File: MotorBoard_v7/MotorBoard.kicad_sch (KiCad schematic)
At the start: 4 parts

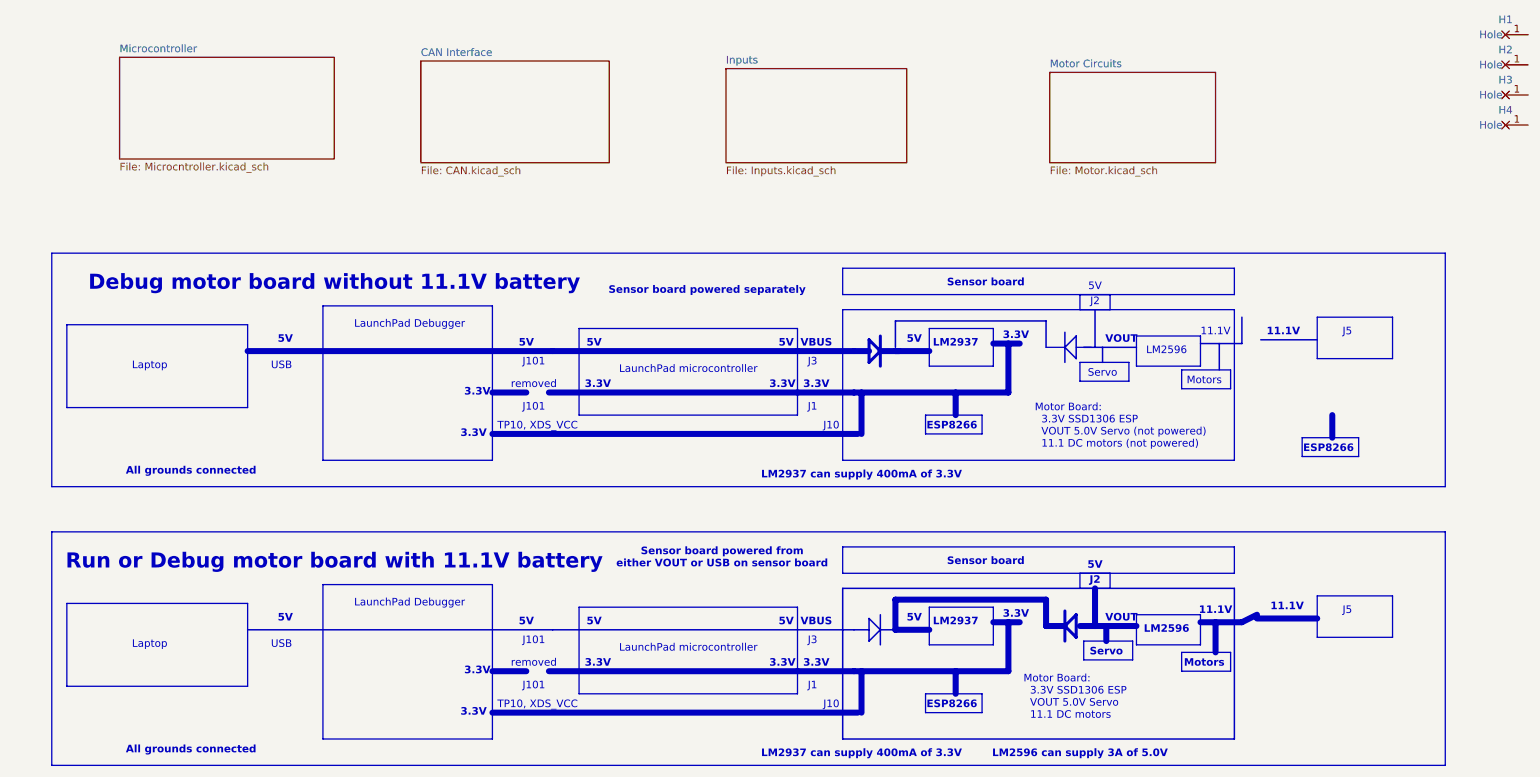
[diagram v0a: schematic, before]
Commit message: added lab 6 update starter files
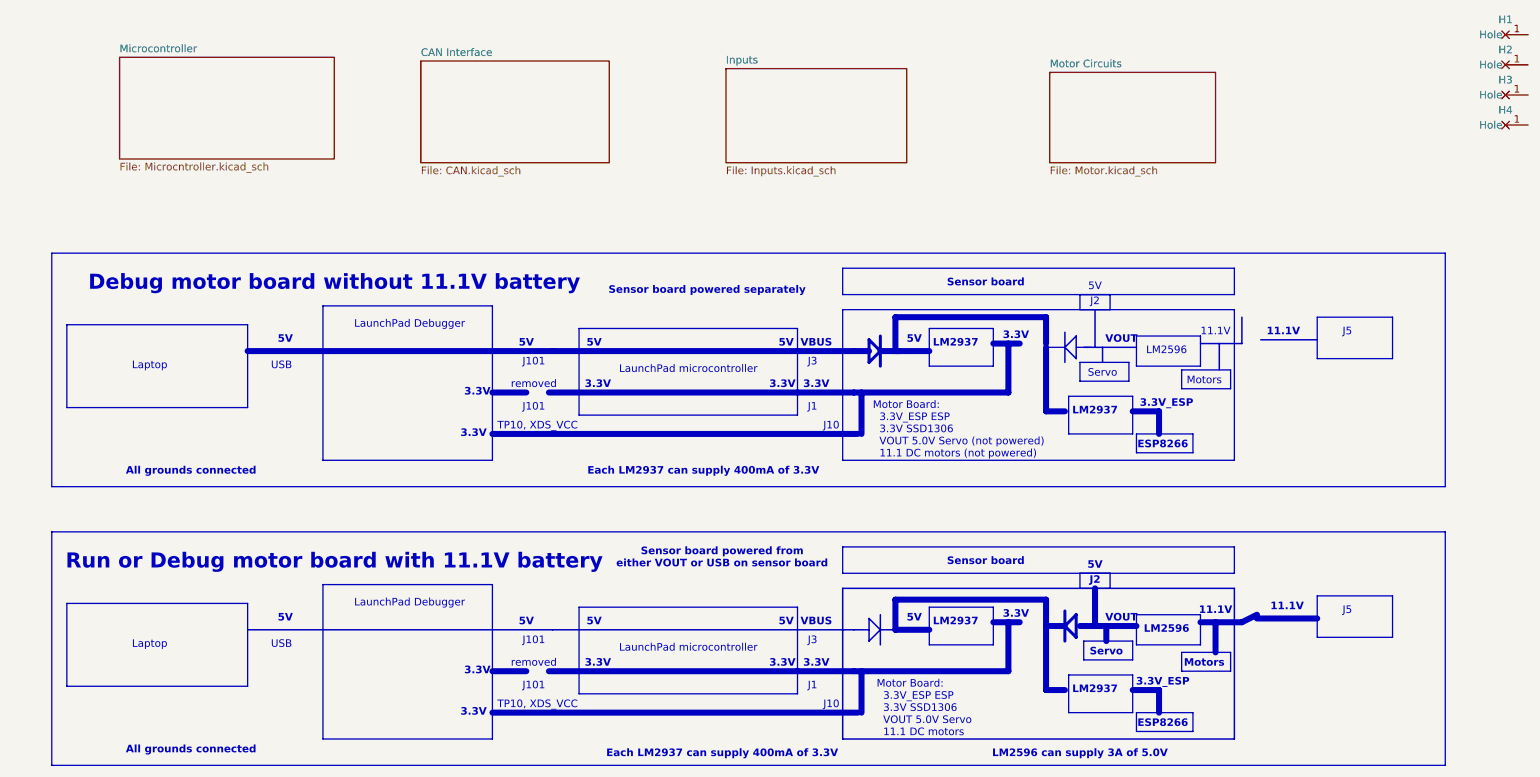
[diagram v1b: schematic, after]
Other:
- note added: "3.3V_ESP"
- note added: "Each LM2937 can supply 400mA of 3.3V"
- note added: "Motor Board: 3.3V_ESP ESP 3.3V SSD1306 VOUT 5.0V Servo (not powered) 11.1 DC motors (not powered)"
- note added: "Motor Board: 3.3V_ESP ESP 3.3V SSD1306 VOUT 5.0V Servo 11.1 DC motors"
- note removed: "LM2937 can supply 400mA of 3.3V"
- note removed: "Motor Board: 3.3V SSD1306 ESP VOUT 5.0V Servo (not powered) 11.1 DC motors (not powered)"
- note removed: "Motor Board: 3.3V SSD1306 ESP VOUT 5.0V Servo 11.1 DC motors"
